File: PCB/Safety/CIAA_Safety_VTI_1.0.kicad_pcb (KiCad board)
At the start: 2 copper layers, 95.9 x 90.2 mm, 119 parts, among them P1 JTAG, SW1 POWER ON RESET, SW2 WARM RESET, U1 SN65HVD1040, U2 PESD1CAN, U3 SN65HVD1040, U4 PESD1CAN, U5 S70FL01GS, U6 DP83848, U7 TMS570LS1227, U8 LM2831, U9 TPS3106K33_DBV_6, X1 50MHZ, Y1 16MHz

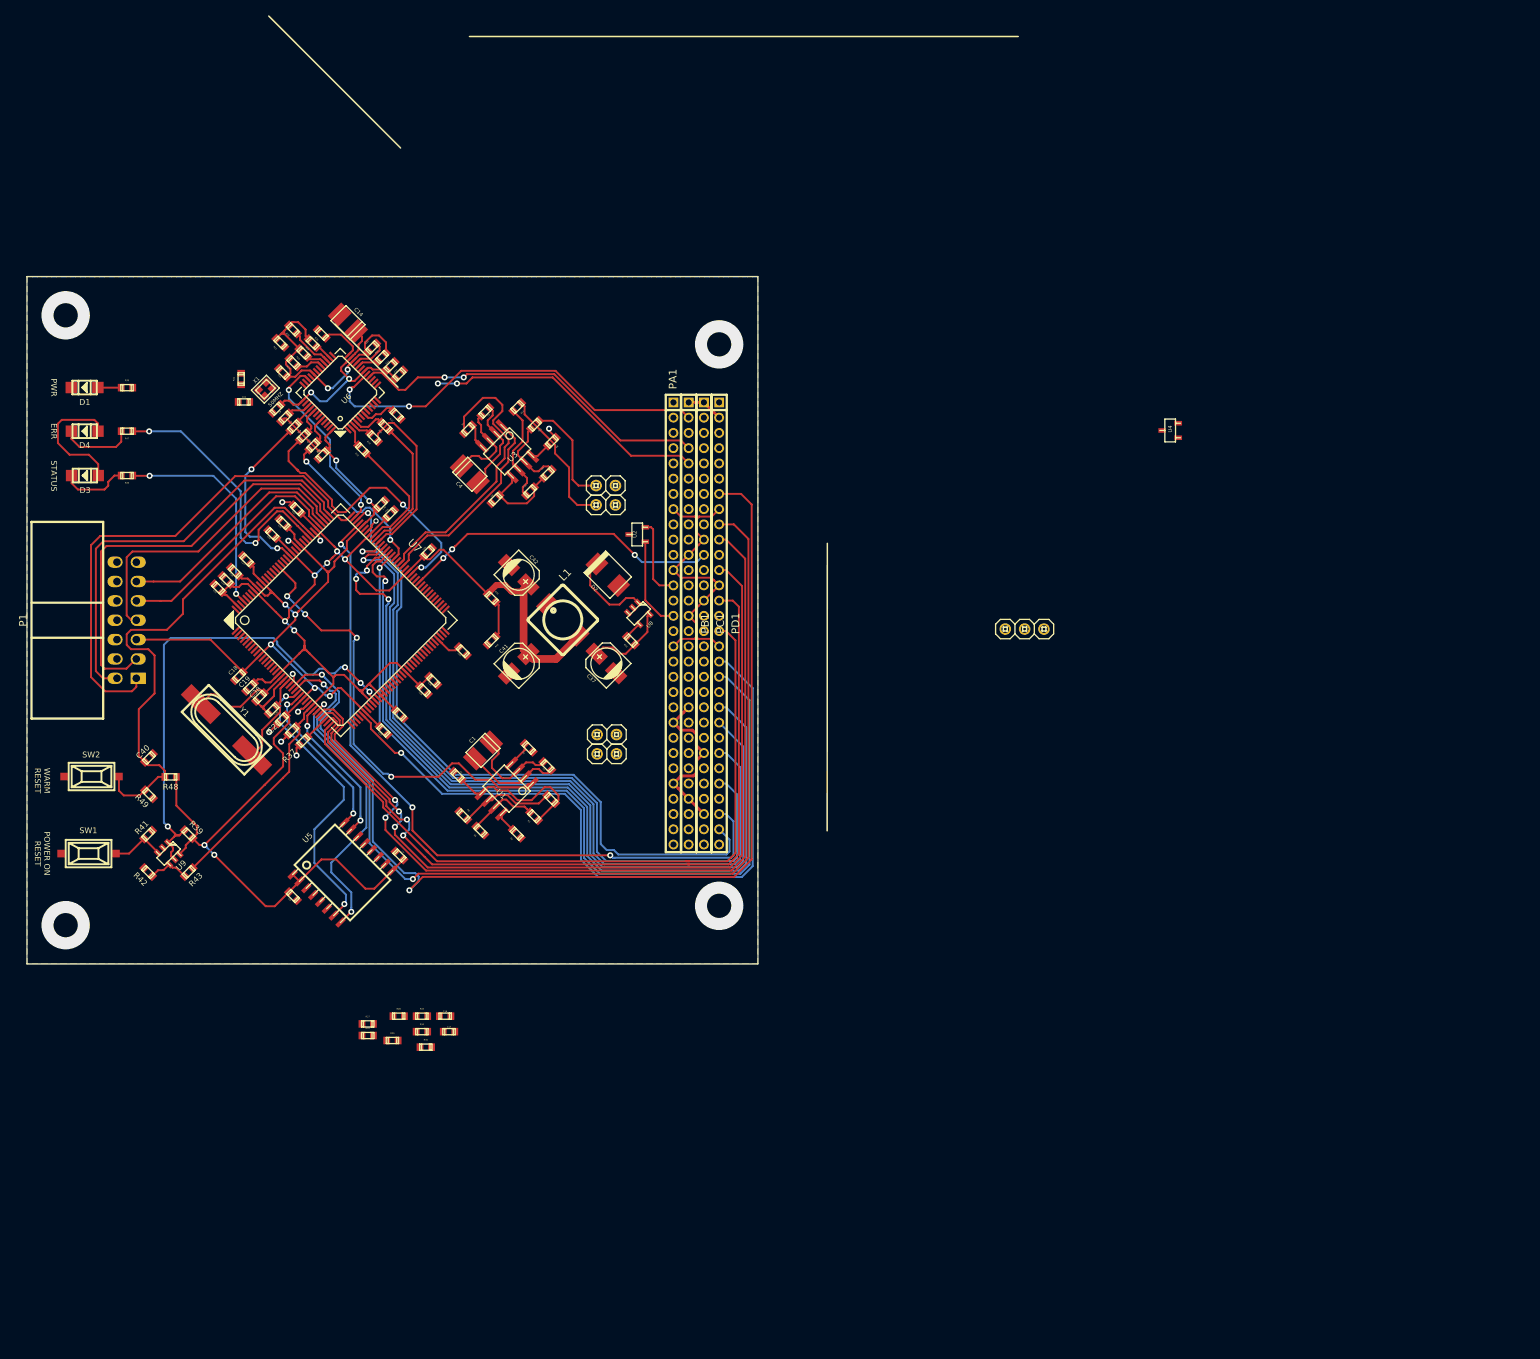
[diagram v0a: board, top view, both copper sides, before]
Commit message: New version (-4) from Fusari,s Drive.
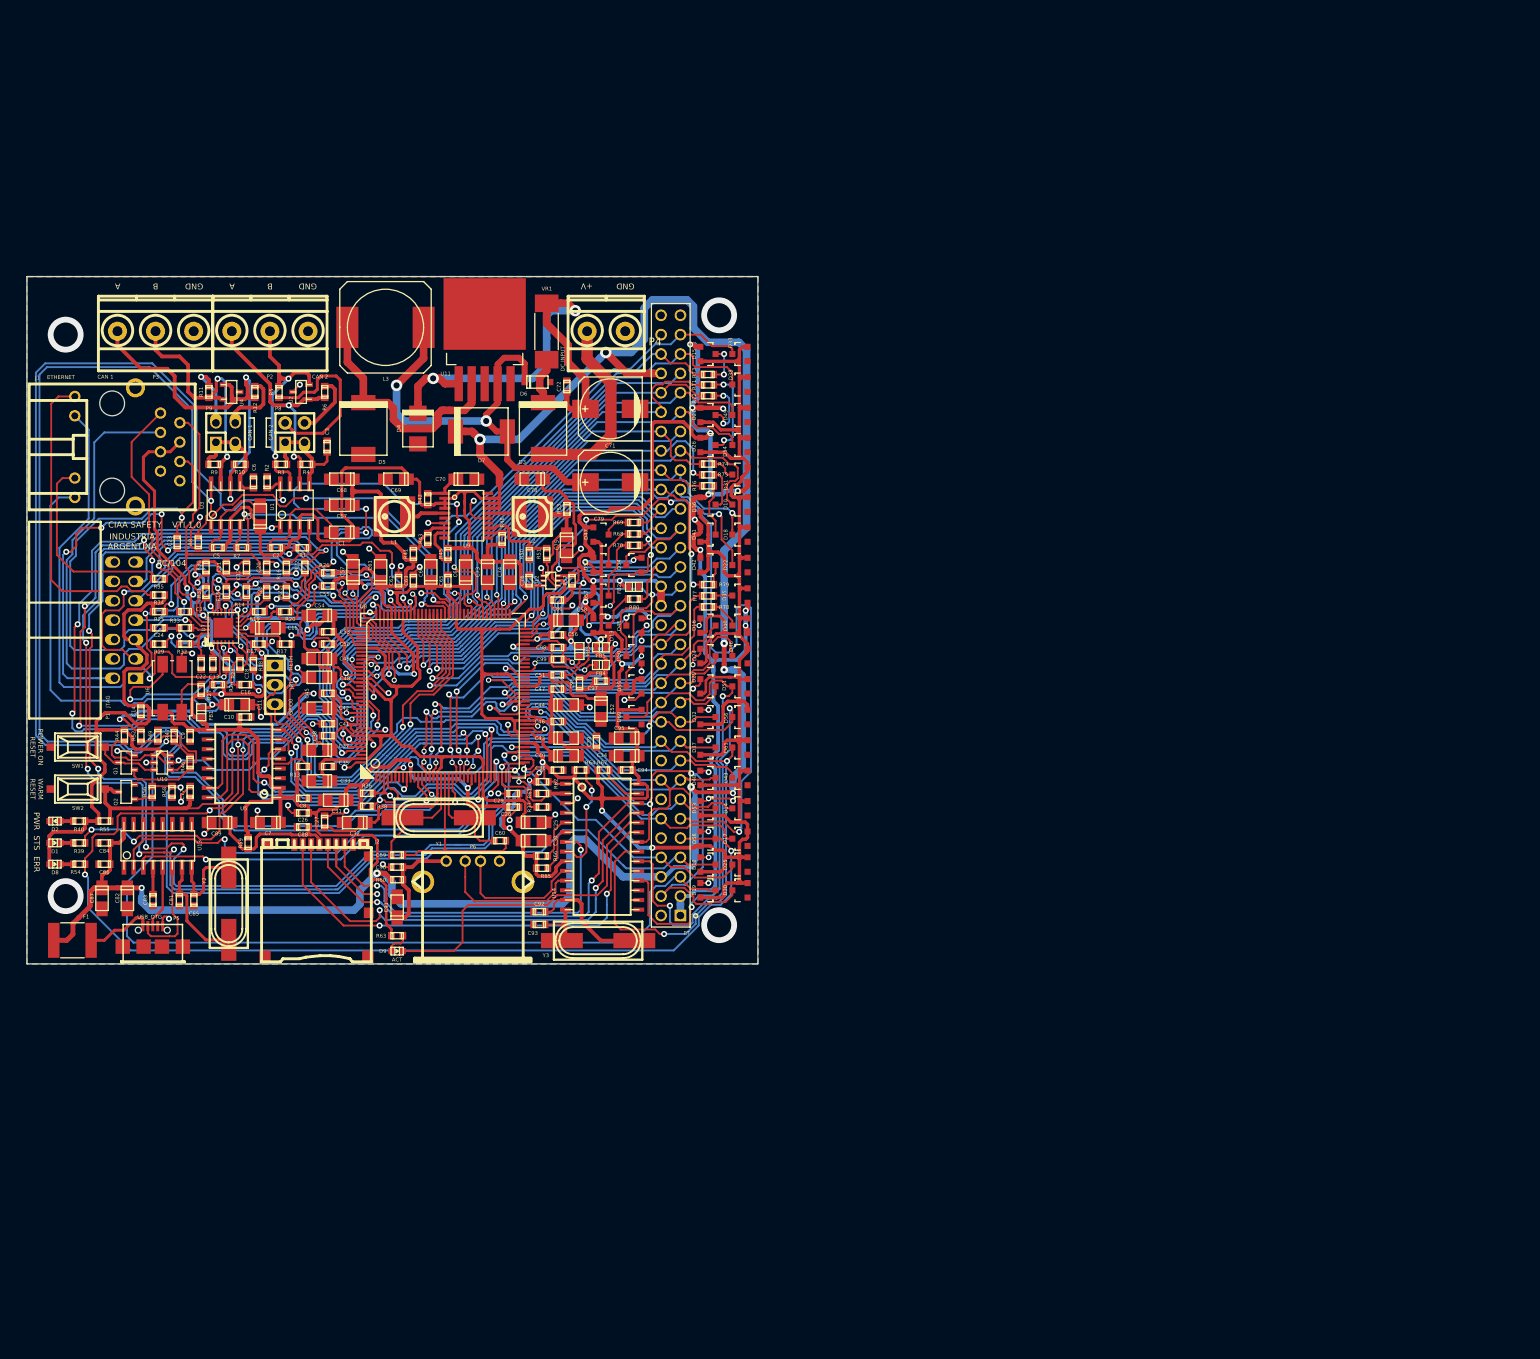
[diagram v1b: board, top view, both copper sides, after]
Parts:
- removed JP2, JP3, JP4, JP5: JUMPER, pin_array_x1:1X02
- removed PA1, PB1, PC1, PD1: CONN_01X30, w_pin_strip:pin_socket_2mm_30
- removed X1: 50MHZ, w_crystal:crystal_fa128
- added C43: 10uF, w_smd_cap:c_tant_A, F.Cu at (70.7, 60.6)
- added C44: 10uF, w_smd_cap:c_tant_A, F.Cu at (70.7, 56.2)
- added C45: 100nF, w_smd_cap:c_0603, F.Cu at (39.5, 54.7)
- added C46: 100nF, w_smd_cap:c_0603, F.Cu at (69.6, 58.4)
- added C47: 100nF, w_smd_cap:c_0603, F.Cu at (69.6, 54.1)
- added C48: 10uF, w_smd_cap:c_tant_A, F.Cu at (38.4, 52.6)
- added C49: 10uF, w_smd_cap:c_tant_A, F.Cu at (38.4, 50.1)
- added C50: 100nF, w_smd_cap:c_0603, F.Cu at (39.5, 48.2)
- added C51: 100nF, w_smd_cap:c_0603, F.Cu at (69.6, 52.2)
- added C52: 10uF, w_smd_cap:c_tant_A, F.Cu at (75.3, 56.7)
- added C53: 100nF, w_smd_cap:c_0603, F.Cu at (39.5, 46.6)
- added C54: 10uF, w_smd_cap:c_tant_A, F.Cu at (38.4, 44.5)
- added C55: 100nF, w_smd_cap:c_0603, F.Cu at (39.5, 40.6)
- added C56: 100nF, w_smd_cap:c_0603, F.Cu at (69.6, 47.0)
- added C57: 10uF, w_smd_cap:c_tant_A, F.Cu at (42.8, 38.7)
- added C58: 10uF, w_smd_cap:c_tant_A, F.Cu at (70.7, 45.1)
- added C59: 33pF, w_smd_cap:c_0603, F.Cu at (48.6, 75.9)
- added C60: 33pF, w_smd_cap:c_0603, F.Cu at (62.1, 74.0)
- added C61: 10uF, w_smd_cap:c_tant_A, F.Cu at (46.4, 38.7)
- added C62: 100nF, w_smd_cap:c_0603, F.Cu at (48.7, 39.9)
- added C63: 100nF, w_smd_cap:c_0603, F.Cu at (50.7, 39.9)
- added C64: 10uF, w_smd_cap:c_tant_A, F.Cu at (53.0, 38.7)
- added C65: 100nF, w_smd_cap:c_0603, F.Cu at (55.2, 39.9)
- added C66: 10uF, w_smd_cap:c_tant_A, F.Cu at (57.6, 38.8)
- added C67: 22uF-6.3V, w_smd_cap:c_tant_A, F.Cu at (41.3, 30.0)
- added C68: 22uF-6.3V, w_smd_cap:c_tant_A, F.Cu at (41.3, 26.6)
- added C69: 22uF-6.3V, w_smd_cap:c_tant_A, F.Cu at (48.4, 26.6)
- added C70: 1uF-6.3V, w_smd_cap:c_tant_A, F.Cu at (57.6, 26.6)
- added C71: 470uF-50V, w_smd_cap:c_elec_8x10, F.Cu at (76.5, 17.4)
- added C72: 100nF, w_smd_cap:c_0603, F.Cu at (70.8, 14.4)
- added C73: 22uF-6.3V, w_smd_cap:c_tant_A, F.Cu at (60.4, 38.8)
- added C74: 10uF-6.3V, w_smd_cap:c_tant_A, F.Cu at (63.3, 38.8)
- added C75: 22uF-6.3V, w_smd_cap:c_tant_A, F.Cu at (70.8, 35.3)
- added C76: 100nF, w_smd_cap:c_0603, F.Cu at (65.9, 39.9)
- added C77: 1000pF, w_smd_cap:c_0603, F.Cu at (21.4, 67.6)
- added C78: 22uF-6.3V, w_smd_cap:c_tant_A, F.Cu at (66.3, 26.6)
- added C79: 330uF-16V, w_smd_cap:c_elec_8x10, F.Cu at (76.5, 27.0)
- added C80: 4700pF, w_smd_cap:c_0603, F.Cu at (69.6, 42.5)
- added C81: 22pF, w_smd_cap:c_0603, F.Cu at (20.0, 81.8)
- added C82: 10uF-6.3V, w_smd_cap:c_tant_A, F.Cu at (13.2, 81.6)
- added C83: 100nF, w_smd_cap:c_0603, F.Cu at (16.5, 81.8)
- added C84: 100nF, w_smd_cap:c_0603, F.Cu at (10.2, 74.3)
- added C85: 22pF, w_smd_cap:c_0603, F.Cu at (21.9, 81.8)
- added C86: 100nF, w_smd_cap:c_0603, F.Cu at (10.2, 77.1)
- added C87: 10uF-6.3V, w_smd_cap:c_tant_A, F.Cu at (9.85, 81.6)
- added C88: 100nF, w_smd_cap:c_0603, F.Cu at (36.2, 72.2)
- added C89: 10uF-6.3V, w_smd_cap:c_tant_A, F.Cu at (25.3, 71.6)
- added C90: 100nF, w_smd_cap:c_0603, F.Cu at (48.6, 77.5)
- added C91: 10uF-6.3V, w_smd_cap:c_tant_A, F.Cu at (48.6, 82.7)
- added C92: 27pF, w_smd_cap:c_0603, F.Cu at (67.2, 83.3)
- added C93: 27pF, w_smd_cap:c_0603, F.Cu at (67.2, 85.0)
- added C94: 100nF, w_smd_cap:c_0603, F.Cu at (78.7, 64.7)
- added C95: 10uF-6.3V, w_smd_cap:c_tant_A, F.Cu at (78.7, 60.6)
- added C96: 10nF, w_smd_cap:c_0603, F.Cu at (72.5, 53.4)
- added C97: 10nF, w_smd_cap:c_0603, F.Cu at (75.3, 53.1)
- added C98: 100nF, w_smd_cap:c_0603, F.Cu at (69.6, 48.7)
- added C99: 10nF, w_smd_cap:c_0603, F.Cu at (69.6, 50.2)
- added D10: BAV199, BAV199:BAV199, F.Cu at (93.5, 29.9)
- added D12: BAV199, BAV199:BAV199, F.Cu at (89.3, 77.1)
- added D13: BAV199, BAV199:BAV199, F.Cu at (75.3, 45.8)
- added D14: BAV199, BAV199:BAV199, F.Cu at (93.5, 69.8)
- added D15: BAV199, BAV199:BAV199, F.Cu at (89.3, 10.2)
- added D16: BAV199, BAV199:BAV199, F.Cu at (89.3, 45.8)
- added D17: BAV199, BAV199:BAV199, F.Cu at (93.5, 73.7)
- added D18: BAV199, BAV199:BAV199, F.Cu at (93.5, 33.8)
- added D19: BAV199, BAV199:BAV199, F.Cu at (89.3, 80.5)
- added D21: BAV199, BAV199:BAV199, F.Cu at (89.3, 18.2)
- added D22: BAV199, BAV199:BAV199, F.Cu at (93.5, 37.8)
- added D24: BAV199, BAV199:BAV199, F.Cu at (89.3, 49.8)
- added D25: BAV199, BAV199:BAV199, F.Cu at (93.5, 77.1)
- added D26: BAV199, BAV199:BAV199, F.Cu at (89.3, 22.1)
- added D29: BAV199, BAV199:BAV199, F.Cu at (89.3, 53.8)
- added D30: BAV199, BAV199:BAV199, F.Cu at (93.5, 80.5)
- added D31: BAV199, BAV199:BAV199, F.Cu at (93.5, 26.0)
- added D32: BAV199, BAV199:BAV199, F.Cu at (89.3, 57.8)
- added D33: BAV199, BAV199:BAV199, F.Cu at (93.5, 10.2)
- added D34: BAV199, BAV199:BAV199, F.Cu at (79.6, 37.8)
- added D35: BAV199, BAV199:BAV199, F.Cu at (93.5, 41.8)
- added D36: BAV199, BAV199:BAV199, F.Cu at (89.3, 29.9)
- added D37: BAV199, BAV199:BAV199, F.Cu at (89.3, 61.8)
- added D38: BAV199, BAV199:BAV199, F.Cu at (93.5, 14.2)
- added D40: BAV199, BAV199:BAV199, F.Cu at (93.5, 45.8)
- added D41: BAV199, BAV199:BAV199, F.Cu at (89.3, 33.8)
- added D42: BAV199, BAV199:BAV199, F.Cu at (89.3, 37.8)
- added D43: BAV199, BAV199:BAV199, F.Cu at (93.5, 65.8)
- added D45: BAV199, BAV199:BAV199, F.Cu at (79.6, 45.8)
- added D46: BAV199, BAV199:BAV199, F.Cu at (93.5, 49.8)
- added D47: BAV199, BAV199:BAV199, F.Cu at (75.3, 33.8)
- added D48: BAV199, BAV199:BAV199, F.Cu at (89.3, 65.8)
- added D49: BAV199, BAV199:BAV199, F.Cu at (93.5, 18.2)
- added D5: MBRS540T3G, w_smd_diode:do214ab, F.Cu at (44.1, 19.9)
- added D50: BAV199, BAV199:BAV199, F.Cu at (79.6, 49.8)
- added D51: BAV199, BAV199:BAV199, F.Cu at (93.5, 53.8)
- added D52: BAV199, BAV199:BAV199, F.Cu at (75.3, 37.8)
- added D53: BAV199, BAV199:BAV199, F.Cu at (89.3, 69.8)
- added D54: BAV199, BAV199:BAV199, F.Cu at (93.5, 22.1)
- added D55: BAV199, BAV199:BAV199, F.Cu at (79.6, 53.8)
- added D56: BAV199, BAV199:BAV199, F.Cu at (93.5, 57.8)
- added D57: BAV199, BAV199:BAV199, F.Cu at (75.3, 41.8)
- added D58: BAV199, BAV199:BAV199, F.Cu at (89.3, 73.7)
- added D6: MMSZ5V6T1G, w_smd_diode:sod123, F.Cu at (67.0, 13.8)
- added D60: BAV199, BAV199:BAV199, F.Cu at (79.6, 57.8)
- added D61: BAV199, BAV199:BAV199, F.Cu at (93.5, 61.8)
- added D7: MURS360, w_smd_diode:do214ab, F.Cu at (59.6, 20.3)
- added D8: ERR, w_smd_leds:Led_0603, F.Cu at (3.68, 77.1)
- added D9: ACT, w_smd_leds:Led_0603, F.Cu at (48.6, 88.5)
- added F1: MF-SMDF050, MF-SMDF050:MF-SMDF050, F.Cu at (5.97, 87.1)
- added FB1: BK1608HS220-T, w_smd_inductors:inductor_smd_0603, F.Cu at (22.9, 57.2)
- added FB2: MMZ1608B601C, w_smd_inductors:inductor_smd_0603, F.Cu at (79.6, 40.7)
- added FB3: ACML0603101, w_smd_inductors:inductor_smd_0603, F.Cu at (72.5, 49.1)
- added FB4: ACML0603101, w_smd_inductors:inductor_smd_0603, F.Cu at (75.3, 51.0)
- added FB5: MMZ1608B601C, w_smd_inductors:inductor_smd_0603, F.Cu at (75.3, 48.6)
- added G***: LOGO, w_logo:Logo_ciaa_safety, B.Cu at (72.4, 19.0)
- added G***: LOGO, w_logo:Logo_gstr, B.Cu at (72.7, 37.9)
- added G***: LOGO, w_logo:Logo_citea, B.Cu at (72.7, 56.8)
- added G***: LOGO, w_logo:Logo_unrc, B.Cu at (16.6, 78.4)
- added G***: LOGO, w_logo:Logo_unca, B.Cu at (32.5, 78.4)
- added G***: LOGO, w_logo:Logo_faa, B.Cu at (25.3, 63.1)
- added G***: LOGO, w_logo:Logo_silk_OSHW_6x6mm, B.Cu at (69.8, 70.1)
- added G***: LOGO, w_logo:Logo_silk_WEEE_3.4x5mm, B.Cu at (76.8, 70.9)
- added J1: HR911105A, HR911105A:HR911105A, F.Cu at (11.2, 22.4)
- added J2: SD-CON, w_conn_misc:microsd_socket, F.Cu at (38.0, 81.9)
- added L2: 1uH-3.1A, w_smd_inductors:inductor_smd_4.8x2.8mm, F.Cu at (66.3, 31.5)
- added L3: 47uH, Inductors:SELF-WE-PD-XXL, F.Cu at (47.0, 6.66)
- added P2: CAN 2, w_conn_mkds:mkds_1,5-3, F.Cu at (31.9, 7.17)
- added P3: CAN 1, w_conn_mkds:mkds_1,5-3, F.Cu at (16.9, 7.17)
- added P4: DC INPUT, w_conn_mkds:mkds_1,5-2, F.Cu at (76.0, 7.17)
- added P5: USB_OTG, w_conn_pc:conn_usb_B_micro_smd-2, F.Cu at (16.5, 87.9)
- added P6: USB_A, w_conn_pc:conn_usb_A, F.Cu at (58.5, 82.7)
- added P7: CONN_02X32, Bus ISA 8 bits:bus_ISA_8bits, F.Cu at (84.5, 85.3)
- added P8: CAN2, w_pin_strip:pin_socket_2x2, F.Cu at (35.1, 20.5)
- added P9: CAN1, w_pin_strip:pin_socket_2x2, F.Cu at (26.1, 20.5)
- added Q1: NDS7002A, w_smd_trans:sot23, F.Cu at (13.0, 63.8)
- added Q2: NDS7002A, w_smd_trans:sot23, F.Cu at (13.0, 67.6)
- added R50: 10K, w_smd_resistors:r_0603, F.Cu at (65.9, 36.4)
- added R51: 5.76K, w_smd_resistors:r_0603, F.Cu at (68.2, 36.4)
- added R52: 2.2K, w_smd_resistors:r_0603, F.Cu at (14.9, 60.2)
- added R53: 0.010, w_smd_resistors:r_0603, F.Cu at (70.8, 30.5)
- added R54: 2.2K, w_smd_resistors:r_0603, F.Cu at (6.86, 77.1)
- added R55: 2.2K, w_smd_resistors:r_0603, F.Cu at (10.2, 71.4)
- added R56: 10K, w_smd_resistors:r_0603, F.Cu at (16.4, 67.6)
- added R57: 31.6K, w_smd_resistors:r_0603, F.Cu at (71.5, 39.9)
- added R58: 330K, w_smd_resistors:r_0603, F.Cu at (19.0, 67.6)
- added R59: 1K, w_smd_resistors:r_0603, F.Cu at (29.0, 74.3)
- added R60: 100, w_smd_resistors:r_0603, F.Cu at (48.6, 79.1)
- added R61: 1K, w_smd_resistors:r_0603, F.Cu at (67.6, 67.8)
- added R62: 1K, w_smd_resistors:r_0603, F.Cu at (67.6, 66.3)
- added R63: 2.2K, w_smd_resistors:r_0603, F.Cu at (48.6, 86.5)
- added R64: 1K, w_smd_resistors:r_0603, F.Cu at (72.6, 64.7)
- added R65: 1K, w_smd_resistors:r_0603, F.Cu at (67.6, 77.6)
- added R66: 1K, w_smd_resistors:r_0603, F.Cu at (67.6, 76.0)
- added R67: 1K, w_smd_resistors:r_0603, F.Cu at (75.6, 64.7)
- added R68: 10K, w_smd_resistors:r_0603, F.Cu at (79.6, 33.8)
- added R69: 10K, w_smd_resistors:r_0603, F.Cu at (79.6, 32.3)
- added R70: 10K, w_smd_resistors:r_0603, F.Cu at (79.6, 35.3)
- added R71: 10K, w_smd_resistors:r_0603, F.Cu at (89.3, 14.2)
- added R72: 10K, w_smd_resistors:r_0603, F.Cu at (89.3, 15.6)
- added R73: 10K, w_smd_resistors:r_0603, F.Cu at (89.3, 12.8)
- added R74: 10K, w_smd_resistors:r_0603, F.Cu at (89.3, 24.6)
- added R75: 10K, w_smd_resistors:r_0603, F.Cu at (89.3, 26.0)
- added R76: 10K, w_smd_resistors:r_0603, F.Cu at (89.3, 27.4)
- added R77: 10K, w_smd_resistors:r_0603, F.Cu at (89.3, 41.9)
- added R78: 10K, w_smd_resistors:r_0603, F.Cu at (89.3, 43.3)
- added R79: 10K, w_smd_resistors:r_0603, F.Cu at (89.3, 40.4)
- added R80: 10K, w_smd_resistors:r_0603, F.Cu at (79.6, 42.3)
- added U10: TPS3106K33_DBV_6, w_smd_trans:sot23-6, F.Cu at (17.7, 63.8)
- added U11: LM2596S-5.0, TO_SOT_Packages_SMD:TO-263-5Lead, F.Cu at (60.0, 14.1)
- added U12: INA210_DCK_6, w_smd_trans:sc70-6, F.Cu at (68.7, 39.9)
- added U13: CH340G, w_smd_dil:so-16, F.Cu at (17.2, 74.7)
- added U14: CH376S, w_smd_dil:soic-28, F.Cu at (75.5, 74.8)
- added VR1: MF-SM300, MF-SM300:MF-SM300, F.Cu at (68.2, 7.21)
- added Y2: 12MHz, w_crystal:hc-49_smd, F.Cu at (26.5, 82.3)
- added Y3: 12MHz, w_crystal:hc-49_smd, F.Cu at (74.9, 87.1)
- C1, C4: footprint w_smd_cap:c_tant_B -> w_smd_cap:c_tant_A
- C11, C15, C7: value 100nF -> 10uF-6.3V; footprint w_smd_cap:c_0603 -> w_smd_cap:c_tant_A
- C14: value 10uF-16V -> 100nF; footprint w_smd_cap:c_tant_B -> w_smd_cap:c_0603
- C16: value 100nF -> 470pF
- C19, C20, C22, C23: value 100nF -> 18pF
- C25, C30, C31, C32, C33, C34: value 100nF -> 10uF; footprint w_smd_cap:c_0603 -> w_smd_cap:c_tant_A
- C37, C42: value 22uF-6.3V -> 10uF; footprint w_smd_cap:c_elec_4x5.3 -> w_smd_cap:c_tant_A
- C38, C39: value 33pF -> 100nF
- C40: value 1000pF -> 10uF; footprint w_smd_cap:c_0603 -> w_smd_cap:c_tant_A
- C41: value 22uF-6.3V -> 100nF; footprint w_smd_cap:c_elec_4x5.3 -> w_smd_cap:c_0603
- D1: value PWR -> STATUS; footprint w_smd_leds:Led_1206 -> w_smd_leds:Led_0603
- D2: value 1N5822 -> PWR; footprint w_smd_diode:do214aa -> w_smd_leds:Led_0603
- D3: value STATUS -> MURS360; footprint w_smd_leds:Led_1206 -> w_smd_diode:do214ab
- D4: value ERR -> P6SMB33CA; footprint w_smd_leds:Led_1206 -> w_smd_diode:do214aa
- JP1: footprint pin_array_x1:1X03 -> w_pin_strip:pin_strip_3
- L1: value 1.6uH-2A -> 1uH-3.1A; footprint w_smd_inductors:inductor_smd_6.5x4.8mm -> w_smd_inductors:inductor_smd_4.8x2.8mm
- R13, R23, R26, R38, R43, R46: value 2.2K -> 10K
- R14, R15, R16: value 33 -> 0
- R17, R18, R19, R20: value 33 -> 22
- R21: value 1.5K -> 0
- R22: value 2.2K -> 0
- R24: value 1.5K -> 10K
- R25: value 2.2K -> 1K5
- R27: value 330 -> 100K
- R28: value 330 -> 24.9
- R29: value 4.87K -> 12.1K
- R30, R31: value 2.2K -> 49,9
- R32: value 10K -> 49,9
- R33: value 49.9 -> 49,9
- R34, R35: value 49.9 -> 270
- R36: value 49.9 -> 10K
- R40: value 100K -> 2.2K
- R41: value 2.2K -> 31.6K
- R42: value 2.2K -> 4.99
- R44: value 10K -> 2.2K
- R45: value 10K -> 49.9K
- R47: value 2.2K -> 330K
- R48: value 2.2K -> 49.9K
- U6: value DP83848 -> Si502; footprint w_smd_lqfp:lqfp48 -> Crystals:Crystal_SMD_7050_4Pads
- U7: value TMS570LS1227 -> LAN8720A-CP; footprint w_smd_lqfp:TQFP-144 -> w_smd_qfn:qfn-24
- U8: value LM2831 -> TMS570LS1227; footprint w_smd_trans:sot23-5 -> w_smd_lqfp:TQFP-144
- U9: value TPS3106K33_DBV_6 -> LM26420; footprint w_smd_trans:sot23-6 -> w_smd_dil:tssop-20
- Y1: footprint w_crystal:crystal_hc-49%2fsmd -> w_crystal:hc-49_smd
- moved U4 123.2 mm to (26.8, 15.1), turned to 270 degrees
- moved JP1 98.6 mm to (32.5, 53.6), turned to 270 degrees
- moved D2 79.4 mm to (3.68, 71.4), turned to 180 degrees
- moved R40 76.1 mm to (6.86, 71.4), turned to 0 degrees
- moved R35 70.7 mm to (17.3, 39.7), turned to 180 degrees
- moved R34 66.9 mm to (17.3, 41.8), turned to 180 degrees
- moved R5 63.3 mm to (33.1, 15.1), turned to 90 degrees
- moved R38 63.3 mm to (44.6, 69.5), turned to 180 degrees
- moved R16 61.5 mm to (34.0, 38.2), turned to 270 degrees
- moved R42 61.1 mm to (52.6, 29.2), turned to 90 degrees
- moved D3 60.4 mm to (67.7, 19.9), turned to 90 degrees
- moved D1 59.9 mm to (3.68, 74.3), turned to 0 degrees
- moved U9 59.1 mm to (57.6, 31.4), turned to 270 degrees
- moved R33 58.6 mm to (20.8, 46.1), turned to 180 degrees
- moved R6 58.5 mm to (39.1, 15.1), turned to 270 degrees
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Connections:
- C11 pad 1: GND -> Net-(C11-Pad1)
- C11 pad 2: +3V3 -> GND
- C12 pad 1: GND -> Net-(C11-Pad1)
- C12 pad 2: /ETHERNET/PFBIN2 -> GND
- C13 pad 1: GND -> Net-(C11-Pad1)
- C13 pad 2: /ETHERNET/PFBIN2 -> GND
- C14 pad 1: /ETHERNET/PFBIN2 -> +3V3
- C16 pad 1: GND -> Net-(C16-Pad1)
- C16 pad 2: +3V3 -> GND
- C17 pad 1: GND -> +3V3
- C17 pad 2: +3V3 -> GND
- C18 pad 1: +3V3 -> Net-(C16-Pad1)
- C19 pad 1: +1V2 -> /ETHERNET/TD+
- C20 pad 1: +3V3 -> /ETHERNET/TD-
- C21 pad 1: +1V2 -> Net-(C11-Pad1)
- C22 pad 1: GND -> /ETHERNET/RD+
- C22 pad 2: +1V2 -> GND
- C23 pad 1: +3V3 -> /ETHERNET/RD-
- C24 pad 1: GND -> Net-(C11-Pad1)
- C24 pad 2: +1V2 -> GND
- C26 pad 1: GND -> +3V3
- C26 pad 2: +3V3 -> GND
- C27 pad 1: GND -> +1V2
- C27 pad 2: +3V3 -> GND
- C28 pad 1: +1V2 -> +3V3
- C29 pad 1: GND -> +1V2
- C29 pad 2: +1V2 -> GND
- C30 pad 1: +1V2 -> +3V3
- C31 pad 1: GND -> +3V3
- C31 pad 2: +3V3 -> GND
- C32 pad 1: GND -> +1V2
- C32 pad 2: +1V2 -> GND
- C33 pad 1: /RM48L952/VCCAD -> +1V2
- C36 pad 1: GND -> +3V3
- C36 pad 2: +1V2 -> GND
- C37 pad 1: +5V -> +1V2
- C38 pad 1: /RM48L952/OSCIN -> GND
- C38 pad 2: /RM48L952/Kelvin_GND -> +1V2
- C39 pad 1: /RM48L952/Kelvin_GND -> +1V2
- C39 pad 2: /RM48L952/OSCOUT -> GND
- C40 pad 1: /RM48L952/nRST -> +1V2
- C41 pad 1: +1V2 -> GND
- C41 pad 2: GND -> +3V3
- C42 pad 1: +1V2 -> +3V3
- C9 pad 1: GND -> +3V3
- C9 pad 2: /ETHERNET/PFBIN2 -> GND
- D1 pad 1: GND -> Net-(D1-Pad1)
- D1 pad 2: Net-(D1-Pad2) -> +3V3
- D2 pad 1: Net-(D2-Pad1) -> GND
- D2 pad 2: GND -> Net-(D2-Pad2)
- D3 pad 2: +3V3 -> Net-(D3-Pad2)
- D4 pad 1: Net-(D4-Pad1) -> GND
- D4 pad 2: +3V3 -> Net-(C71-Pad1)
- JP1 pad 1: /ETHERNET/RESET_N -> /RESET_ETH
- JP1 pad 2: /RM48L952/GPIO0 -> /ISA_GPIO0/RESET_ETH
- JP1 pad 3: /PCI_GPIO0 -> /ISA_GPIO0
- L1 pad 1: Net-(D2-Pad1) -> +3V3
- L1 pad 2: +1V2 -> Net-(L1-Pad2)
- P1 pad 1: /RM48L952/TMS -> /TMS
- P1 pad 11: /RM48L952/TCK -> /TCK
- P1 pad 2: /RM48L952/nTRST -> /nTRST
- P1 pad 3: /RM48L952/TDI -> /TDI
- P1 pad 7: /RM48L952/TDO -> /TDO
- P1 pad 9: /RM48L952/RTCK -> /RTCK
- R13 pad 1: +3V3 -> Net-(R13-Pad1)
- R13 pad 2: Net-(R13-Pad2) -> +3V3
- R14 pad 1: /ETHERNET/RMII_CRS_DV -> Net-(R14-Pad1)
- R14 pad 2: Net-(R14-Pad2) -> /CPU/RMII_TXD[0]
- R15 pad 1: /ETHERNET/RMII_RX_ER -> Net-(R15-Pad1)
- R15 pad 2: Net-(R15-Pad2) -> /CPU/RMII_TXD[1]
- R16 pad 1: /ETHERNET/RMII_RXD[0] -> Net-(R16-Pad1)
- R16 pad 2: Net-(R16-Pad2) -> /CPU/RMII_TXEN
- R17 pad 1: /ETHERNET/RMII_RXD[1] -> Net-(R17-Pad1)
- R17 pad 2: Net-(R17-Pad2) -> /CPU/RMII_RXD[0]
- R18 pad 2: /ETHERNET/RMII_TXEN -> /CPU/RMII_RXD[1]
- R19 pad 2: /ETHERNET/RMII_TXD[0] -> /CPU/RMII_CRS_DV
- R20 pad 2: /ETHERNET/RMII_TXD[1] -> /CPU/RMII_RX_ER
- R21 pad 1: +3V3 -> Net-(R21-Pad1)
- R21 pad 2: /ETHERNET/MDIO -> /CPU/MDIO
- R22 pad 2: +3V3 -> /CPU/MDCLK
- R23 pad 1: +3V3 -> Net-(R23-Pad1)
- R23 pad 2: Net-(R23-Pad2) -> +3V3
- R24 pad 1: +3V3 -> /ETHERNET/LED_100M
- R24 pad 2: /ETHERNET/RESET_N -> +3V3
- R25 pad 1: +3V3 -> Net-(R21-Pad1)
- R25 pad 2: Net-(R25-Pad2) -> +3V3
- R26 pad 1: +3V3 -> Net-(R20-Pad1)
- R26 pad 2: Net-(R26-Pad2) -> +3V3
- R27 pad 1: Net-(R23-Pad2) -> Net-(R27-Pad1)
- R27 pad 2: /ETHERNET/LED_LINK -> +3V3
- R28 pad 1: Net-(R26-Pad2) -> Net-(R28-Pad1)
- R28 pad 2: /ETHERNET/LED_ACT -> /CPU/RMII_REFCLK
- R30 pad 1: +3V3 -> Net-(C11-Pad1)
- R30 pad 2: Net-(R30-Pad2) -> /ETHERNET/TD+
- R31 pad 1: Net-(R31-Pad1) -> Net-(C11-Pad1)
- R31 pad 2: +3V3 -> /ETHERNET/TD-
- R32 pad 1: +3V3 -> Net-(C11-Pad1)
- R32 pad 2: Net-(R32-Pad2) -> /ETHERNET/RD+
- R33 pad 1: /ETHERNET/TD+ -> Net-(C11-Pad1)
- R33 pad 2: +3V3 -> /ETHERNET/RD-
- R34 pad 1: +3V3 -> Net-(J1-Pad12)
- R34 pad 2: /ETHERNET/TD- -> +3V3
- R35 pad 1: /ETHERNET/RD+ -> Net-(J1-Pad10)
- R35 pad 2: +3V3 -> GND
- R36 pad 2: /ETHERNET/RD- -> /ISA_I2C_SCL
- R38 pad 1: +5V -> +3V3
- R38 pad 2: Net-(D1-Pad2) -> /ISA_I2C_SDA
- R39 pad 1: +3V3 -> Net-(D1-Pad1)
- R39 pad 2: /RM48L952/nPORRST -> /CPU/STATUS
- R40 pad 1: Net-(R40-Pad1) -> +3V3
- R40 pad 2: +5V -> Net-(D2-Pad2)
- R41 pad 1: /RM48L952/PCI_MR -> Net-(R41-Pad1)
- R41 pad 2: Net-(R41-Pad2) -> +3V3
- R42 pad 1: Net-(R42-Pad1) -> Net-(C70-Pad1)
- R42 pad 2: GND -> +5V
- R43 pad 1: +1V2 -> Net-(R41-Pad1)
- R43 pad 2: Net-(R42-Pad1) -> GND
- R44 pad 1: Net-(R44-Pad1) -> +3V3
- R44 pad 2: +1V2 -> /CPU/nPORRST
- R45 pad 1: GND -> Net-(R45-Pad1)
- R45 pad 2: Net-(R44-Pad1) -> +5V
- R46 pad 1: Net-(D3-Pad1) -> /ISA_MR
- R46 pad 2: /RM48L952/STATUS -> Net-(Q1-PadG)
- R47 pad 1: Net-(D4-Pad1) -> GND
- R47 pad 2: /RM48L952/PCI_nERROR -> /ISA_MR
- R48 pad 1: +3V3 -> +5V
- R48 pad 2: /RM48L952/nRST -> Net-(R48-Pad2)
- R49 pad 1: /RM48L952/PCI_nRST -> Net-(R49-Pad1)
- R49 pad 2: /RM48L952/nRST -> GND
- SW1 pad 2: Net-(R41-Pad2) -> Net-(Q1-PadD)
- SW2 pad 2: /RM48L952/nRST -> /CPU/nRST
- U5 pad 15: /MEM_FLASH_SPI/SPI4SIMO[0] -> /CPU/SPI4SIMO[0]
- U5 pad 16: /MEM_FLASH_SPI/SPI4CLK -> /CPU/SPI4CLK
- U5 pad 6: Net-(U5-Pad6) -> Net-(R13-Pad1)
- U5 pad 7: /MEM_FLASH_SPI/SPI4NCS[0] -> /CPU/SPI4NCS[0]
- U5 pad 8: /MEM_FLASH_SPI/SPI4SOMI[0] -> /CPU/SPI4SOMI[0]
- U6 pad 1: Net-(U6-Pad1) -> Net-(R27-Pad1)
- U6 pad 2: Net-(R18-Pad1) -> GND
- U6 pad 3: Net-(R19-Pad1) -> Net-(R28-Pad1)
- U6 pad 4: Net-(R20-Pad1) -> +3V3
- U7 pad 1: Net-(U7-Pad1) -> Net-(C11-Pad1)
- U7 pad 10: +3V3 -> Net-(R20-Pad1)
- U7 pad 11: GND -> Net-(R19-Pad1)
- U7 pad 12: /CAN 1/2/CAN1_STB -> Net-(R21-Pad1)
- U7 pad 13: /CAN 1/2/CAN2_STB -> Net-(R22-Pad1)
- U7 pad 14: /RM48L952/GPIO1 -> Net-(R23-Pad1)
- U7 pad 15: /RM48L952/GPIO2 -> /RESET_ETH
- U7 pad 16: /RM48L952/GPIO3 -> Net-(R16-Pad1)
- U7 pad 17: +1V2 -> Net-(R14-Pad1)
- U7 pad 18: /RM48L952/OSCIN -> Net-(R15-Pad1)
- U7 pad 19: /RM48L952/Kelvin_GND -> Net-(C11-Pad1)
- U7 pad 2: Net-(U7-Pad2) -> /ETHERNET/LED_100M
- U7 pad 20: /RM48L952/OSCOUT -> /ETHERNET/TD-
- U7 pad 21: GND -> /ETHERNET/TD+
- U7 pad 22: /RM48L952/GPIO4 -> /ETHERNET/RD-
- U7 pad 23: /RM48L952/GPIO5 -> /ETHERNET/RD+
- U7 pad 24: /MEM_FLASH_SPI/SPI4NCS[0] -> Net-(R29-Pad2)
- U7 pad 25: /MEM_FLASH_SPI/SPI4CLK -> (no net)
- U7 pad 3: /RM48L952/I2C_SCL/GPIO25 -> /ETHERNET/LED_LINK
- U7 pad 4: /RM48L952/I2C_SDA/GPIO26 -> Net-(U7-Pad4)
- U7 pad 5: Net-(U7-Pad5) -> /CPU/RMII_REFCLK
- U7 pad 6: /RM48L952/MIBSPI3NCS[4]/GPIO27 -> Net-(C16-Pad1)
- U7 pad 7: Net-(U7-Pad7) -> Net-(R18-Pad1)
- U7 pad 8: Net-(U7-Pad8) -> Net-(R17-Pad1)
- U7 pad 9: /RM48L952/GPIO0 -> +3V3
- U8 pad 1: Net-(D2-Pad1) -> Net-(U8-Pad1)
- U8 pad 2: GND -> Net-(U8-Pad2)
- U8 pad 3: Net-(R44-Pad1) -> /ISA_I2C_SCL
- U8 pad 4: Net-(R40-Pad1) -> /ISA_I2C_SDA
- U8 pad 5: +5V -> Net-(U8-Pad5)
- U9 pad 1: /RM48L952/nPORRST -> Net-(C70-Pad1)
- U9 pad 2: GND -> +5V
- U9 pad 3: Net-(R41-Pad2) -> +5V
- U9 pad 4: Net-(R42-Pad1) -> +5V
- U9 pad 5: /RM48L952/nPORRST -> Net-(L1-Pad2)
- U9 pad 6: +3V3 -> GND
- Y1 pad 1: /RM48L952/OSCIN -> /CPU/OSCIN
- Y1 pad 2: /RM48L952/OSCOUT -> /CPU/OSCOUT
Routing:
- net +3V3: track 281.1 -> 737.5 mm, vias 11 -> 21
- net +5V: track 61.5 -> 377.8 mm, vias 0 -> 8
- net GNDA: track 0.00 -> 223.4 mm, vias 0 -> 16
- net /CPU/MDIO: track 0.00 -> 188.7 mm, vias 0 -> 8
- net /ISA_nERROR: track 0.00 -> 178.9 mm, vias 0 -> 5
- net /CAN 1/2/CAN2_STB: track 2.64 -> 171.8 mm, vias 0 -> 2
- net GND: track 16.3 -> 175.3 mm, vias 10 -> 67
- net /CAN 1/2/CAN1_STB: track 2.58 -> 159.5 mm, vias 0 -> 2
- net /CPU/MDCLK: track 0.00 -> 150.3 mm, vias 0 -> 6
- net /RM48L952/GPIO4: track 139.5 -> 0.00 mm, vias 2 -> 0
- net /RM48L952/GPIO5: track 129.3 -> 0.00 mm, vias 2 -> 0
- net +1V2: track 177.5 -> 306.0 mm, vias 6 -> 4
- net /ISA_MR: track 0.00 -> 116.5 mm, vias 0 -> 1
- net /RM48L952/GPIO6: track 116.5 -> 0.00 mm, vias 2 -> 0
- net /CAN 1/2/CAN2RX: track 0.00 -> 113.2 mm, vias 0 -> 6
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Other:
- net class Default: clearance 0.1524 -> 0.15; trace_width 0.254 -> 0.25
- rule trace_clearance: 0.1524 -> 0.15
- rule trace_min: 0.0508 -> 0.2
- board text added: "+V"
- board text added: "A"
- board text added: "B"
- board text added: "CAN 1"
- board text added: "CAN 2"
- board text added: "CIAA SAFETY"
- board text added: "CIAA SAFETY VTI - 1.0 Plataforma desarrollada en el marco del Proyecto de Desarrollo Tecnológico y Social (PDTS) CIN-CONICET Nº151: “Desarrollo de una Computadora Industrial Abierta Argentina (CIAA) para aplicaciones que requieran de seguridad funcional certificada” 2016 - 2017"
- board text added: "ETHERNET"
- board text added: "GND"
- board text added: "GPIO0"
- board text added: "INDUSTRIA ARGENTINA"
- board text added: "JTAG"
- board text added: "PC/104"
- board text added: "RETH"
- board text added: "STS"
- board text added: "VTI 1.0"
- board text removed: "STATUS"

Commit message: Added Diego Fusari's last version. Changes in texts, title blocks and sheet names.
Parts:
- moved C1 112.2 mm to (141.9, 83.3)
- moved C2 112.2 mm to (133.2, 85.3)
- moved C26 112.2 mm to (136.8, 120.1)
- moved C35 112.2 mm to (140.0, 114.0)
- moved C38 112.2 mm to (140.0, 110.0)
- moved C41 112.2 mm to (140.0, 108.4)
- moved C45 112.2 mm to (140.0, 104.4)
- moved C50 112.2 mm to (140.0, 98.0)
- moved C53 112.2 mm to (140.0, 96.3)
- moved C55 112.2 mm to (140.0, 90.3)
- moved C59 112.2 mm to (149.1, 125.6)
- moved C60 112.2 mm to (162.6, 123.7)
- moved C65 112.2 mm to (155.8, 89.6)
- moved C67 112.2 mm to (141.9, 79.7)
- moved C68 112.2 mm to (141.9, 76.3)
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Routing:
- net (no net): vias 5 -> 7
